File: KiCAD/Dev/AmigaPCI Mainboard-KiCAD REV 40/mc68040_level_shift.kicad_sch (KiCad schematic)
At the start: 28 parts, among them U800 74LVC1G17, U801 74LVC1G17, U802 SN74LVC16T245DLR, U803 SN74LVC16T245DLR, U804 SN74LVC16T245DLR, U805 SN74LVC16T245DLR, U806 74LVC245, U807 74LVC245, U808 74LVC245, U809 74LVC245, U810 74LVC245, U811 74LVC245

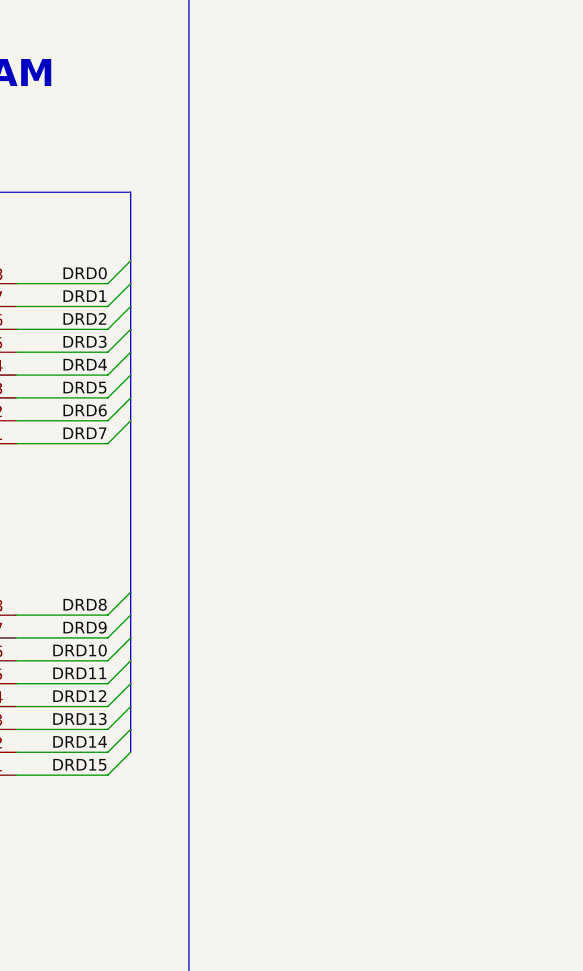
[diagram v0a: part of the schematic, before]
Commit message: Schematic Changes to Clocks 09-JUL-2024
Make changes to support clock generation on CPU local bus card.
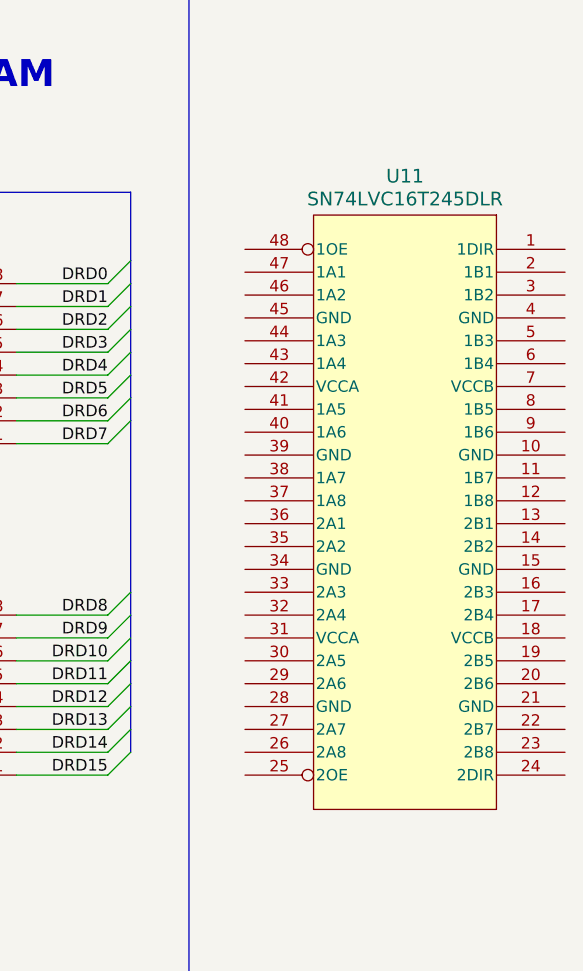
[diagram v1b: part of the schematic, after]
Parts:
- added U11: SN74LVC16T245DLR, AmigaPCI:48-BSSOP, symbol AmigaPCI-Symbols:SN74LVC16T245DLR
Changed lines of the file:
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@@
 	(title_block
 		(title "AMIGA PCI")
-		(date "2024-07-03")
+		(date "2024-07-09")
 		(rev "4.0")
 	)
@@
 					(unit 1)
 				)
+			)
+		)
+	)
+	(symbol
+		(lib_name "SN74LVC16T245DLR_3")
+		(lib_id "AmigaPCI-Symbols:SN74LVC16T245DLR")
+		(at 427.99 74.93 0)
+		(mirror y)
+		(unit 1)
+		(exclude_from_sim no)
+		(in_bom yes)
+		(on_board yes)
+		(dnp no)
+		(property "Reference" "U11"
+			(at 427.99 38.862 0)
+			(effects
+				(font
+					(size 1.524 1.524)
+				)
+			)
+		)
+		(property "Value" "SN74LVC16T245DLR"
+			(at 427.99 41.402 0)
+			(effects
+				(font
+					(size 1.524 1.524)
+				)
+			)
+		)
+		(property "Footprint" "AmigaPCI:48-BSSOP"
+			(at 397.51 91.44 0)
+			(effects
+				(font
+					(size 1.27 1.27)
+					(italic yes)
+				)
+				(hide yes)
+			)
+		)
+		(property "Datasheet" "SN74LVC16T245DLR"
+			(at 397.51 93.98 0)
+			(effects
+				(font
+					(size 1.27 1.27)
+					(italic yes)
+				)
+				(hide yes)
+			)
+		)
+		(property "Description" ""
+			(at 427.99 74.93 0)
+			(effects
+				(font
+					(size 1.27 1.27)
+				)
+				(hide yes)
+			)
+		)
+		(pin "3"
+		)
+		(pin "8"
+		)
+		(pin "42"
+		)
+		(pin "6"
+		)
+		(pin "36"
+		)
+		(pin "34"
+		)
+		(pin "35"
+		)
+		(pin "32"
+		)
+		(pin "39"
+		)
+		(pin "41"
+		)
+		(pin "7"
+		)
+		(pin "37"
+		)
+		(pin "44"
+		)
+		(pin "30"
+		)
+		(pin "28"
+		)
+		(pin "18"
+		)
+		(pin "14"
+		)
+		(pin "13"
+		)
+		(pin "12"
+		)
+		(pin "21"
+		)
+		(pin "19"
+		)
+		(pin "10"
+		)
+		(pin "11"
+		)
+		(pin "1"
+		)
+		(pin "20"
+		)
+		(pin "2"
+		)
+		(pin "15"
+		)
+		(pin "16"
+		)
+		(pin "5"
+		)
+		(pin "29"
+		)
+		(pin "31"
+		)
+		(pin "48"
+		)
+		(pin "40"
+		)
+		(pin "38"
+		)
+		(pin "47"
+		)
+		(pin "9"
+		)
+		(pin "43"
+		)
+		(pin "26"
+		)
+		(pin "24"
+		)
+		(pin "23"
+		)
+		(pin "33"
+		)
+		(pin "4"
+		)
+		(pin "17"
+		)
+		(pin "22"
+		)
+		(pin "27"
+		)
+		(pin "25"
+		)
+		(pin "45"
+		)
+		(pin "46"
+		)
+		(instances
+			(project "AmigaPCI Mainboard"
+				(path "/72453515-27fe-4336-91f3-e3c8054f7767/3746f476-970c-4acb-b19d-33c43fff35fb"
+					(reference "U11")
+					(unit 1)
+				)

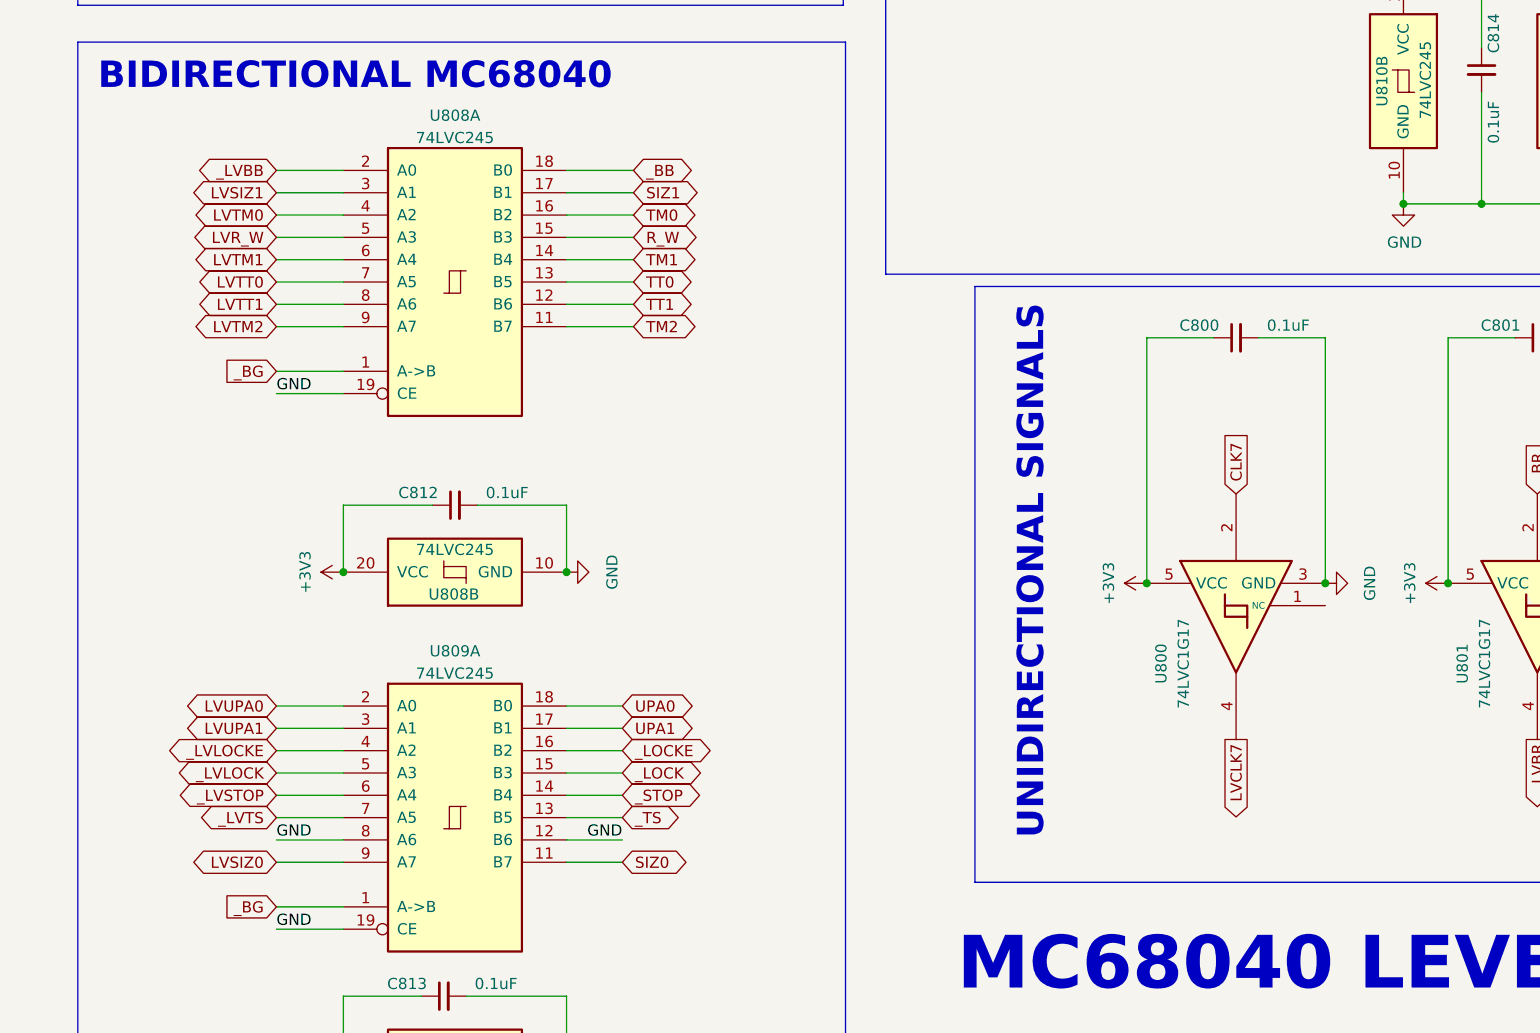
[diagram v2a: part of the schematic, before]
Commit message: AmigaPCI Rev 4.0 Routing
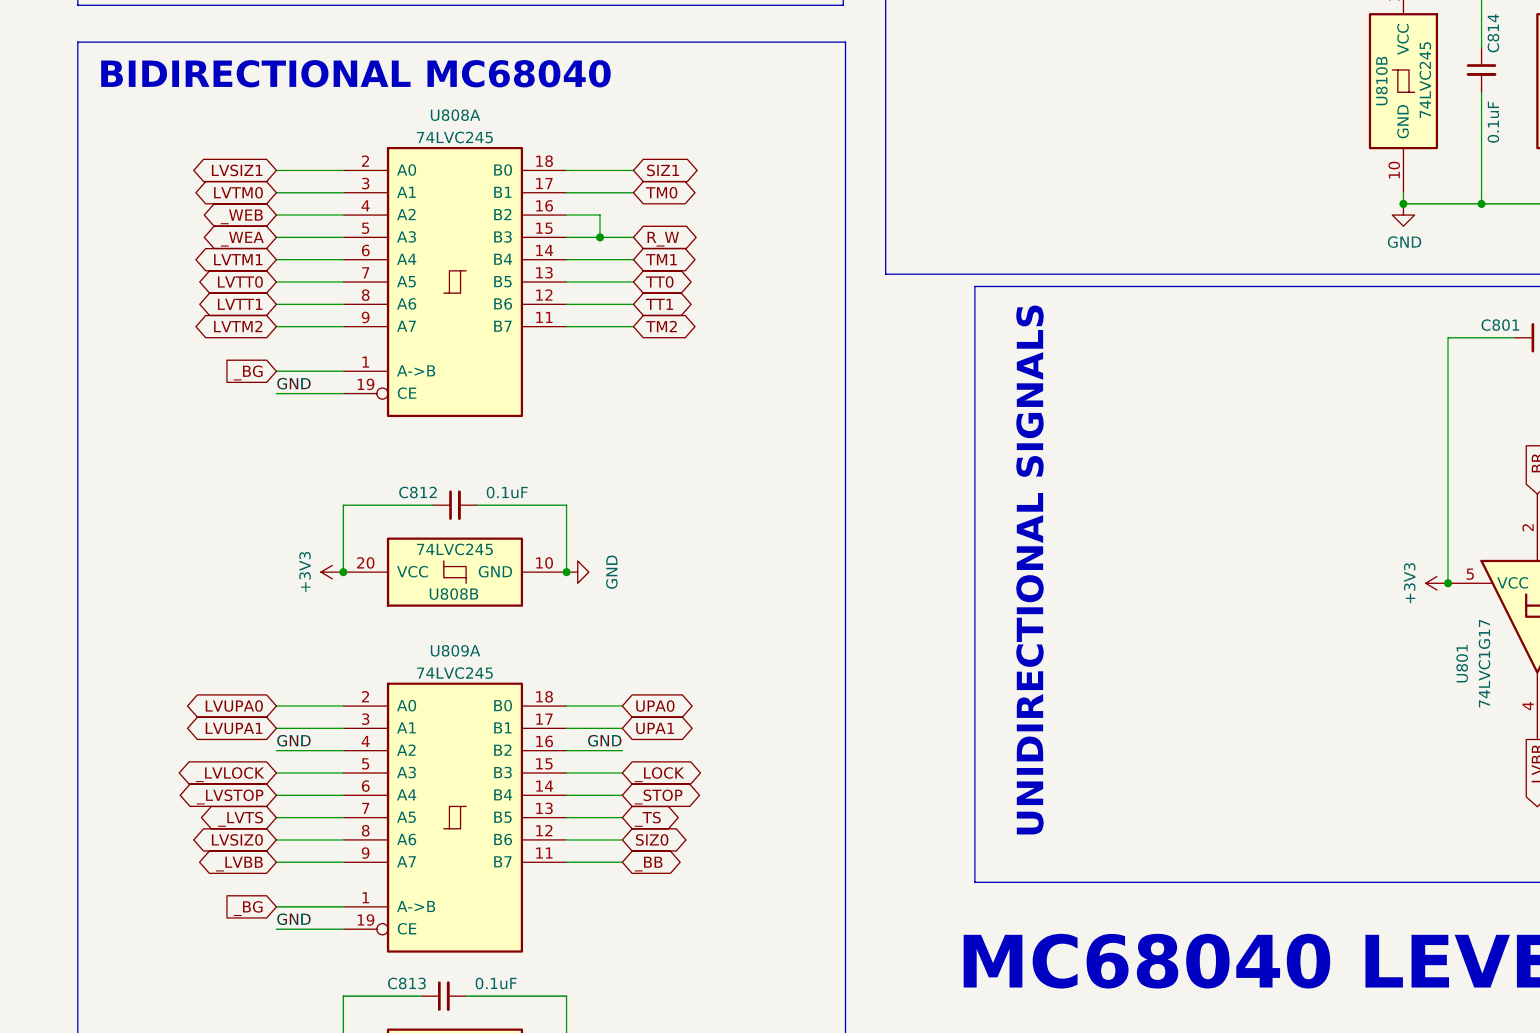
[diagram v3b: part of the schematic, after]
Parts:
- removed C800: 0.1uF, Capacitor_SMD:C_0603_1608Metric, symbol Device:C_Small
- removed U800: 74LVC1G17, Package_TO_SOT_SMD:SOT-23-5, symbol 74xGxx:74LVC1G17
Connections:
- net _LOCKE is gone; now on net GND: U809.16 (B2)
- net _LVLOCKE is gone; now on net GND: U809.4 (A2)
- net GND: no longer U809.12 (B6), U809.8 (A6)
- net LVSIZ0: now also U809.8 (A6); no longer U809.9 (A7)
- net LVSIZ1: now also U808.2 (A0); no longer U808.3 (A1)
- net LVTM0: now also U808.3 (A1); no longer U808.4 (A2)
- net R_W: now also U808.16 (B2)
- net SIZ0: now also U809.12 (B6); no longer U809.11 (B7)
- net SIZ1: now also U808.18 (B0); no longer U808.17 (B1)
- net TM0: now also U808.17 (B1); no longer U808.16 (B2)
- net _BB: now also U809.11 (B7); no longer U808.18 (B0)
- net _LVBB: now also U809.9 (A7); no longer U808.2 (A0)
- net LVR_W renamed _WEA
- new net _WEB: U808.4 (A2)

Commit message: AmigaPCI Mainboard REV 4.0 Routing
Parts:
- removed U11: SN74LVC16T245DLR, AmigaPCI:48-BSSOP, symbol AmigaPCI-Symbols:SN74LVC16T245DLR
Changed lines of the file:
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@@
 	(title_block
 		(title "AMIGA PCI")
-		(date "2024-07-17")
+		(date "2024-07-31")
 		(rev "4.0")
 	)
@@
 					(unit 1)
 				)
-			)
-		)
-	)
-	(symbol
-		(lib_name "SN74LVC16T245DLR_3")
-		(lib_id "AmigaPCI-Symbols:SN74LVC16T245DLR")
-		(at 427.99 74.93 0)
-		(mirror y)
-		(unit 1)
-		(exclude_from_sim no)
-		(in_bom yes)
-		(on_board yes)
-		(dnp no)
-		(property "Reference" "U11"
-			(at 427.99 38.862 0)
-			(effects
-				(font
-					(size 1.524 1.524)
-				)
-			)
-		)
-		(property "Value" "SN74LVC16T245DLR"
-			(at 427.99 41.402 0)
-			(effects
-				(font
-					(size 1.524 1.524)
-				)
-			)
-		)
-		(property "Footprint" "AmigaPCI:48-BSSOP"
-			(at 397.51 91.44 0)
-			(effects
-				(font
-					(size 1.27 1.27)
-					(italic yes)
-				)
-				(hide yes)
-			)
-		)
-		(property "Datasheet" "SN74LVC16T245DLR"
-			(at 397.51 93.98 0)
-			(effects
-				(font
-					(size 1.27 1.27)
-					(italic yes)
-				)
-				(hide yes)
-			)
-		)
-		(property "Description" ""
-			(at 427.99 74.93 0)
-			(effects
-				(font
-					(size 1.27 1.27)
-				)
-				(hide yes)
-			)
-		)
-		(pin "3"
-		)
-		(pin "8"
-		)
-		(pin "42"
-		)
-		(pin "6"
-		)
-		(pin "36"
-		)
-		(pin "34"
-		)
-		(pin "35"
-		)
-		(pin "32"
-		)
-		(pin "39"
-		)
-		(pin "41"
-		)
-		(pin "7"
-		)
-		(pin "37"
-		)
-		(pin "44"
-		)
-		(pin "30"
-		)
-		(pin "28"
-		)
-		(pin "18"
-		)
-		(pin "14"
-		)
-		(pin "13"
-		)
-		(pin "12"
-		)
-		(pin "21"
-		)
-		(pin "19"
-		)
-		(pin "10"
-		)
-		(pin "11"
-		)
-		(pin "1"
-		)
-		(pin "20"
-		)
-		(pin "2"
-		)
-		(pin "15"
-		)
-		(pin "16"
-		)
-		(pin "5"
-		)
-		(pin "29"
-		)
-		(pin "31"
-		)
-		(pin "48"
-		)
-		(pin "40"
-		)
-		(pin "38"
-		)
-		(pin "47"
-		)
-		(pin "9"
-		)
-		(pin "43"
-		)
-		(pin "26"
-		)
-		(pin "24"
-		)
-		(pin "23"
-		)
-		(pin "33"
-		)
-		(pin "4"
-		)
-		(pin "17"
-		)
-		(pin "22"
-		)
-		(pin "27"
-		)
-		(pin "25"
-		)
-		(pin "45"
-		)
-		(pin "46"
-		)
-		(instances
-			(project "AmigaPCI Mainboard"
-				(path "/72453515-27fe-4336-91f3-e3c8054f7767/3746f476-970c-4acb-b19d-33c43fff35fb"
-					(reference "U11")
-					(unit 1)
-				)
